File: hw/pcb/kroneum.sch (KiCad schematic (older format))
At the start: 22 parts, among them J1 USB_B_Micro, SW1 Boot_Mode_Btn, SW2 Ctrl_One_Btn, SW3 Reset_Btn, SW4 Ctrl_Ten_Btn, U1 STM32F042F4Px, Y1 16 Mhz

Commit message: Initial firmware.
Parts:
- R1: value 1k -> 470
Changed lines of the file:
@@
 P 5700 2650
 F 0 "R1" V 5493 2650 50  0000 C CNN
-F 1 "1k" V 5584 2650 50  0000 C CNN
+F 1 "470" V 5584 2650 50  0000 C CNN
 F 2 "Resistor_SMD:R_0805_2012Metric_Pad1.15x1.40mm_HandSolder" V 5630 2650 50  0001 C CNN
 F 3 "~" H 5700 2650 50  0001 C CNN

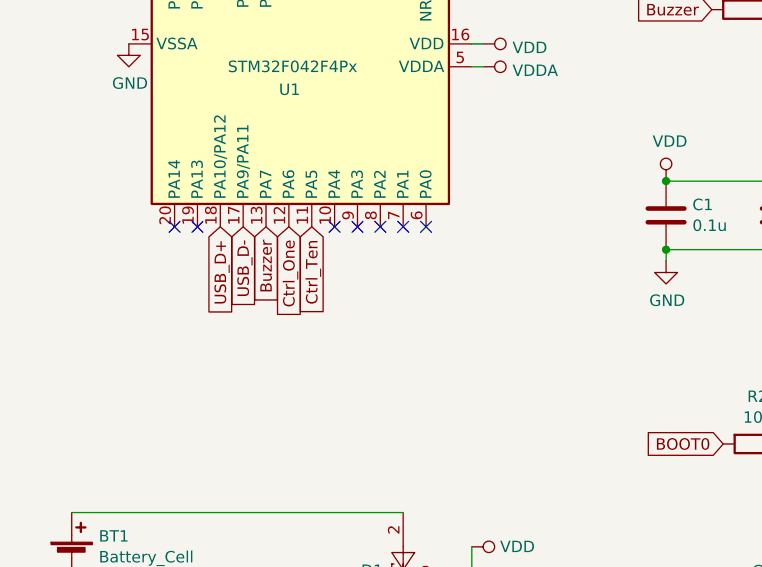
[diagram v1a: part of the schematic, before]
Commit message: hw: switch `ten-1` button from PA5 to PA0 to be able to wake up device from stand-by mode.
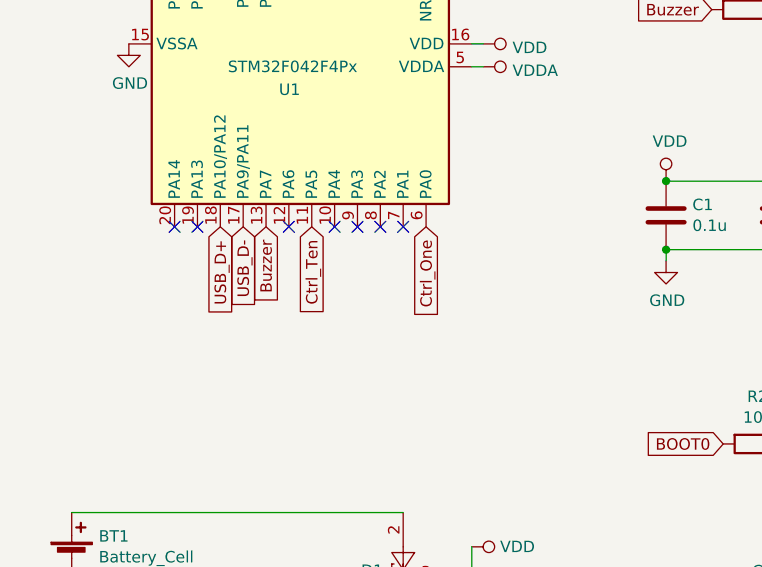
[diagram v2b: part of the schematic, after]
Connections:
- net Ctrl_One: now also U1.6 (PA0); no longer U1.12 (PA6)
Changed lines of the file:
@@
 Text GLabel 5600 4550 0    50   Input ~ 0
 BOOT0
-Text GLabel 3700 3600 3    50   Input ~ 0
+Text GLabel 4300 3600 3    50   Input ~ 0
 Ctrl_One
 Text GLabel 3800 3600 3    50   Input ~ 0
 Ctrl_Ten
-NoConn ~ 4300 3600
+NoConn ~ 3700 3600
 NoConn ~ 4200 3600
 NoConn ~ 4100 3600

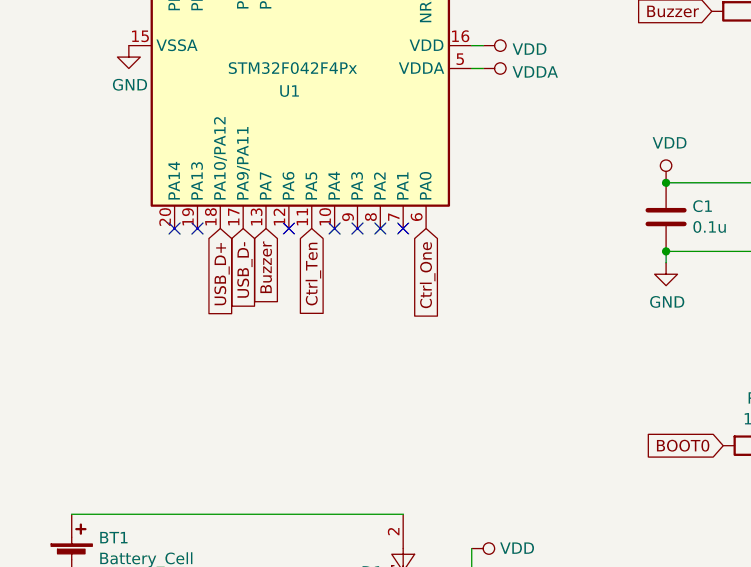
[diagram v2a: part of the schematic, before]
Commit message: hw: connect x-button to PA2 instead of PA5 (to have access to wkup4).
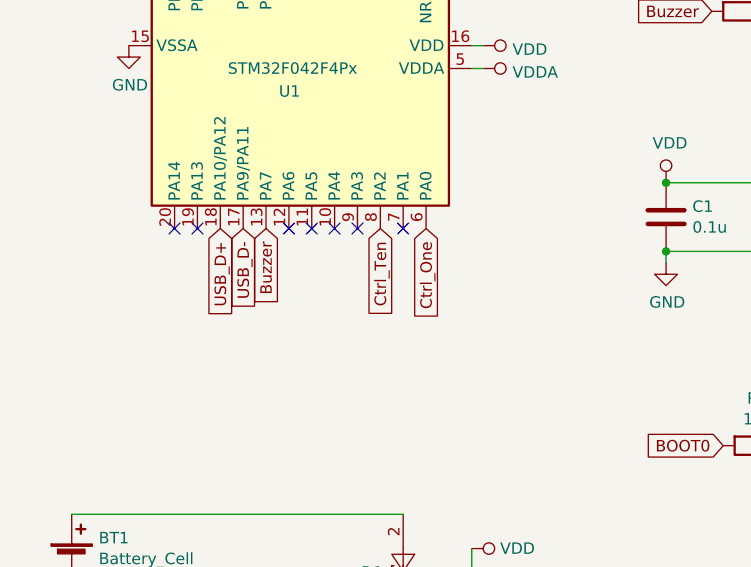
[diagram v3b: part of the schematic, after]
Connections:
- net Ctrl_Ten: now also U1.8 (PA2); no longer U1.11 (PA5)
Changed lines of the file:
@@
 Text GLabel 4300 3600 3    50   Input ~ 0
 Ctrl_One
-Text GLabel 3800 3600 3    50   Input ~ 0
+Text GLabel 4100 3600 3    50   Input ~ 0
 Ctrl_Ten
 NoConn ~ 3700 3600
+NoConn ~ 3800 3600
 NoConn ~ 4200 3600
-NoConn ~ 4100 3600
 NoConn ~ 4000 3600
 NoConn ~ 3900 3600

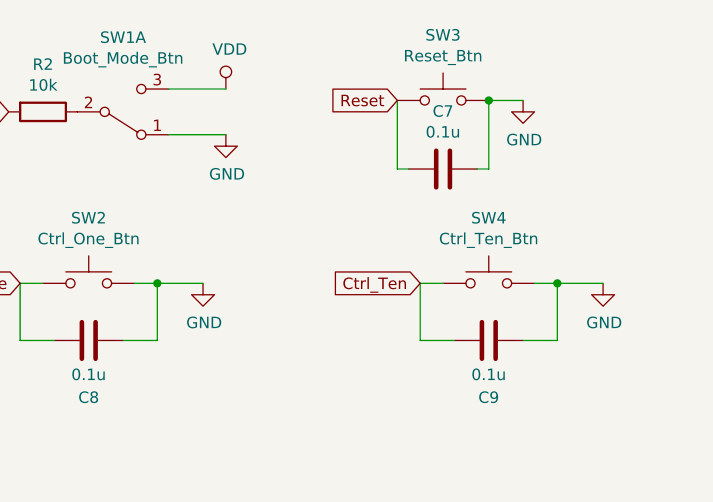
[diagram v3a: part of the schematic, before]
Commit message: hw: use default pull-downs for PA0 and PA2.
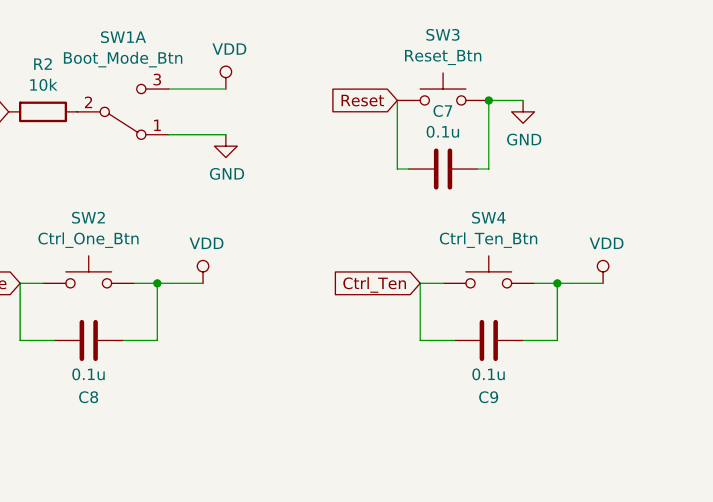
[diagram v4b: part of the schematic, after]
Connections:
- net GND: no longer C8.1, C9.1, SW2.2, SW4.2
- net VDD: now also C8.1, C9.1, SW2.2, SW4.2
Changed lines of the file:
@@
 Connection ~ 6250 5300
-$Comp
-L power:GND #PWR018
-U 1 1 5C211816
-P 6450 5300
-F 0 "#PWR018" H 6450 5050 50  0001 C CNN
-F 1 "GND" H 6455 5127 50  0000 C CNN
-F 2 "" H 6450 5300 50  0001 C CNN
-F 3 "" H 6450 5300 50  0001 C CNN
-	1    6450 5300
-	1    0    0    -1
-$EndComp
 $Comp
 L Switch:SW_Push SW4
@@
 	8000 5300 8200 5300
 Connection ~ 8000 5300
-$Comp
-L power:GND #PWR021
-U 1 1 5C211C21
-P 8200 5300
-F 0 "#PWR021" H 8200 5050 50  0001 C CNN
-F 1 "GND" H 8205 5127 50  0000 C CNN
-F 2 "" H 8200 5300 50  0001 C CNN
-F 3 "" H 8200 5300 50  0001 C CNN
-	1    8200 5300
-	1    0    0    -1
-$EndComp
 $Comp
 L power:VDD #PWR0102
@@
 	0    1    1    0
 $EndComp
+$Comp
+L power:VDD #PWR09
+U 1 1 5C3B98E7
+P 6450 5300
+F 0 "#PWR09" H 6450 5150 50  0001 C CNN
+F 1 "VDD" H 6467 5473 50  0000 C CNN
+F 2 "" H 6450 5300 50  0001 C CNN
+F 3 "" H 6450 5300 50  0001 C CNN
+	1    6450 5300
+	1    0    0    -1
+$EndComp
+$Comp
+L power:VDD #PWR010
+U 1 1 5C3B994A
+P 8200 5300
+F 0 "#PWR010" H 8200 5150 50  0001 C CNN
+F 1 "VDD" H 8217 5473 50  0000 C CNN
+F 2 "" H 8200 5300 50  0001 C CNN
+F 3 "" H 8200 5300 50  0001 C CNN
+	1    8200 5300
+	1    0    0    -1
+$EndComp
 $EndSCHEMATC
